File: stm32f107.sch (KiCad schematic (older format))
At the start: 12 parts, among them U5 STM32F107RCTx, Y2 Crystal

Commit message: a bunch of stuff I guess. mostly layout.
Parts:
- C23: renamed from C22; footprint (none) -> Capacitors_SMD:C_0603
- C24: renamed from C23; footprint (none) -> Capacitors_SMD:C_0603
- C25: renamed from C24; footprint (none) -> Capacitors_SMD:C_0603
- C26: renamed from C25; footprint (none) -> Capacitors_SMD:C_0603
- C27: renamed from C26; footprint (none) -> Capacitors_SMD:C_0603
- C28: renamed from C27; footprint (none) -> Capacitors_SMD:C_0603
- C29: renamed from C28; footprint (none) -> Capacitors_SMD:C_0603
- C30: renamed from C29; footprint (none) -> Capacitors_SMD:C_0603
- C31: renamed from C30; footprint (none) -> Capacitors_SMD:C_0603
- C32: renamed from C31; footprint (none) -> Capacitors_SMD:C_0603
- U5: footprint Package_QFP:LQFP-64_10x10mm_P0.5mm -> Housings_QFP:LQFP-64_10x10mm_Pitch0.5mm
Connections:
- net OSC1: now reaches C31.1, U5.5 (PD0), Y2.1
- net OSC2: now reaches C32.1, U5.6 (PD1), Y2.2

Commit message: layout
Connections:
- net OTG_FS_DM renamed OTG_FS_N
- net OTG_FS_DP renamed OTG_FS_P
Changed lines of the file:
@@
 	6400 3300 6700 3300
 Text HLabel 6700 3300 2    50   BiDi ~ 0
-OTG_FS_DM
+OTG_FS_N
 Wire Wire Line
 	6400 3400 6700 3400
 Text HLabel 6700 3400 2    50   BiDi ~ 0
-OTG_FS_DP
+OTG_FS_P
 Wire Wire Line
 	6400 3500 6700 3500

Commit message: pcb updates or something
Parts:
- removed Y2: Crystal, symbol Device:Crystal
- added Y2: Crystal_GND24, Crystals:Crystal_SMD_3225-4pin_3.2x2.5mm, symbol Device:Crystal_GND24
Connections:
- net GND: now also C32.1, Y2.2, Y2.4; no longer C32.2
- net OSC1: now also Y2.1
- net OSC2: now also C32.2, Y2.3; no longer C32.1
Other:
- moved on the sheet: C31, C32

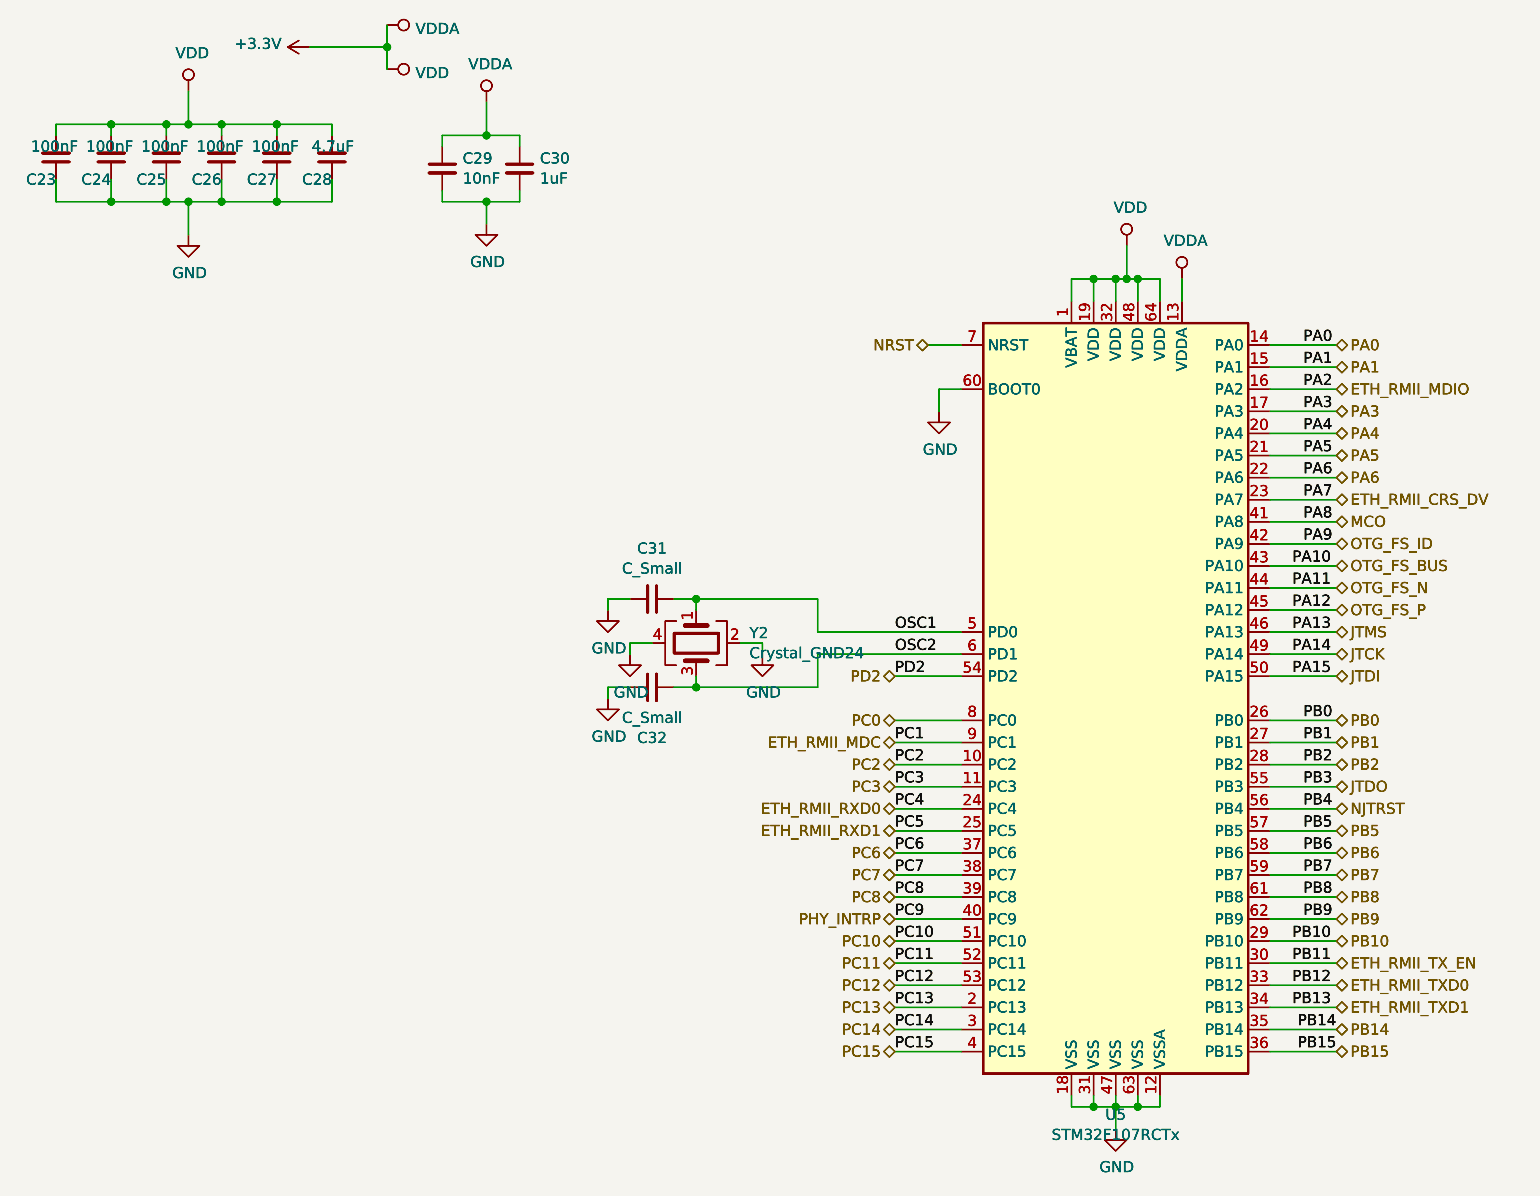
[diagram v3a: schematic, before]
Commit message: redirected 3D models for custom footprints on PCB
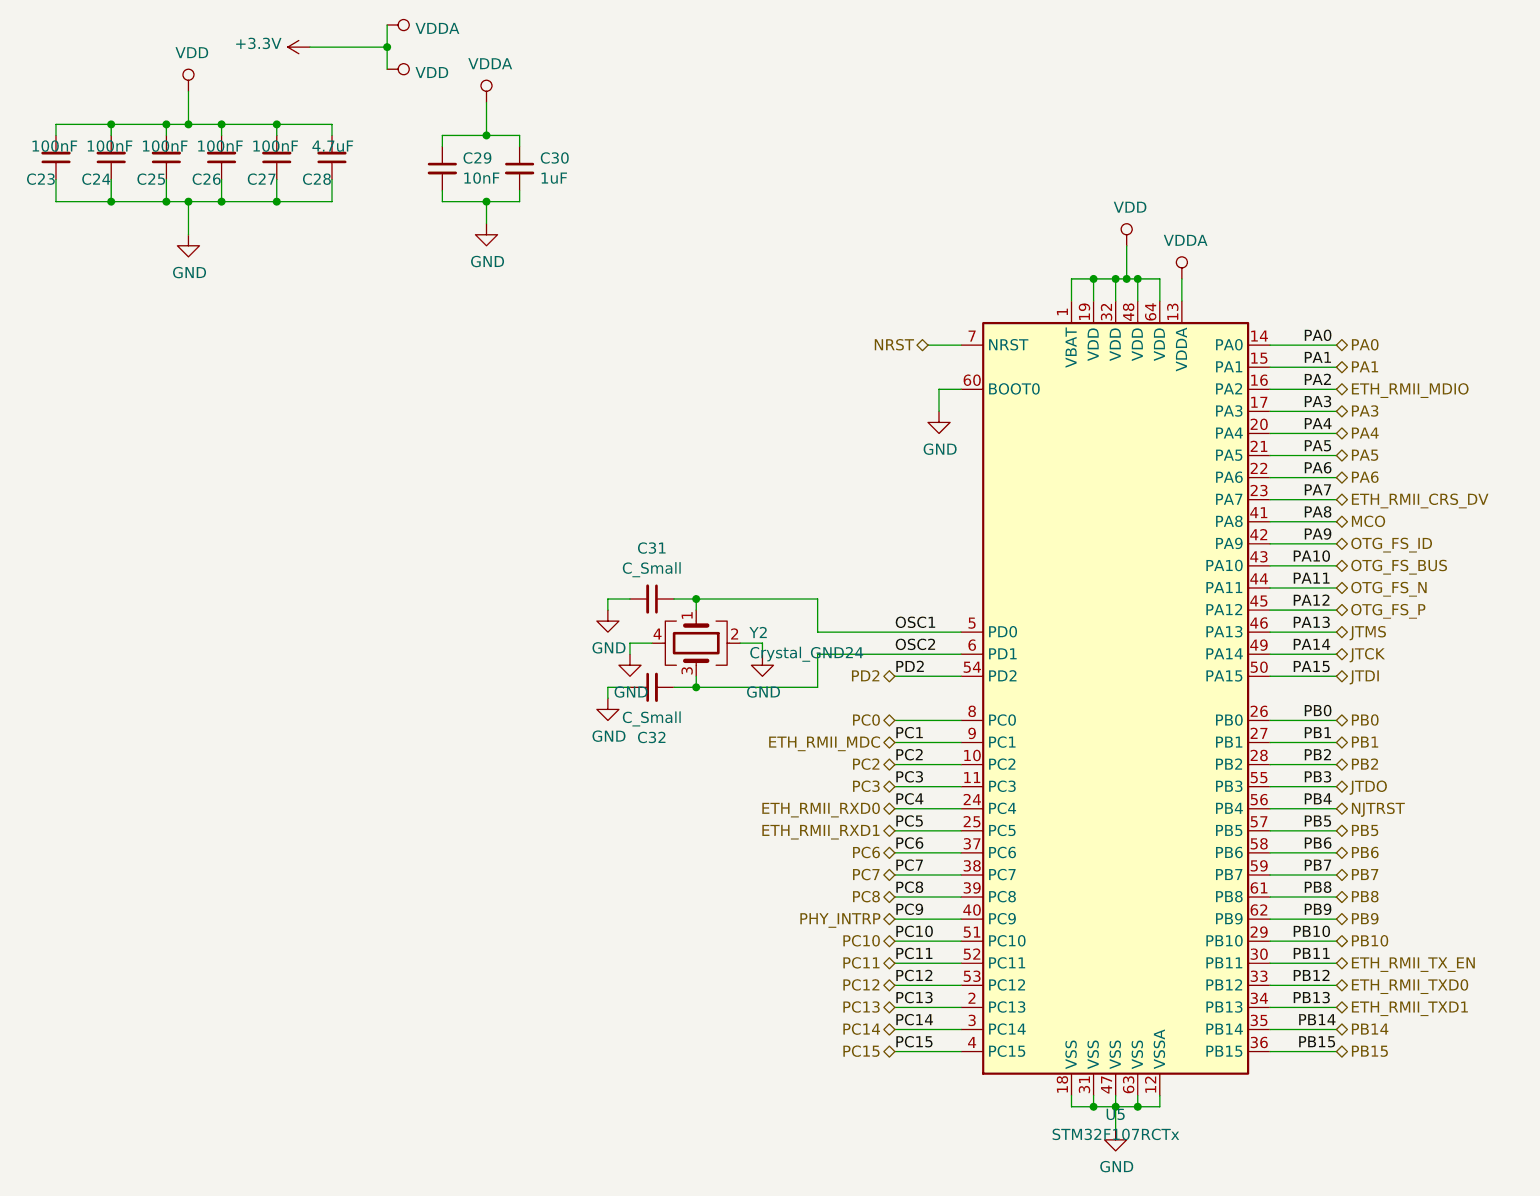
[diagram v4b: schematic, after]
